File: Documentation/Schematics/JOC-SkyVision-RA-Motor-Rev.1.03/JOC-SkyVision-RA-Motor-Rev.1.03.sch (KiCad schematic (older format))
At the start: 18 parts, among them CON1 Conn_01x02_Male, CON2 Conn_01x02_Male, J1 RJ45, J2 RJ45, J3 RJ12 (ST-04 Guiding Port), Q1 4947A Dual P-Channel Mosfet, Q2 4936A Dual N-Channel Mosfet, U1 PIC16F690-ISO, U2_LED Motor Encoder LED, U2_PD Motor Encoder Photodiodes, U3 AZ1117-5.0 (GH15E), U4 TC4426A, X1 20 MHz Crystal

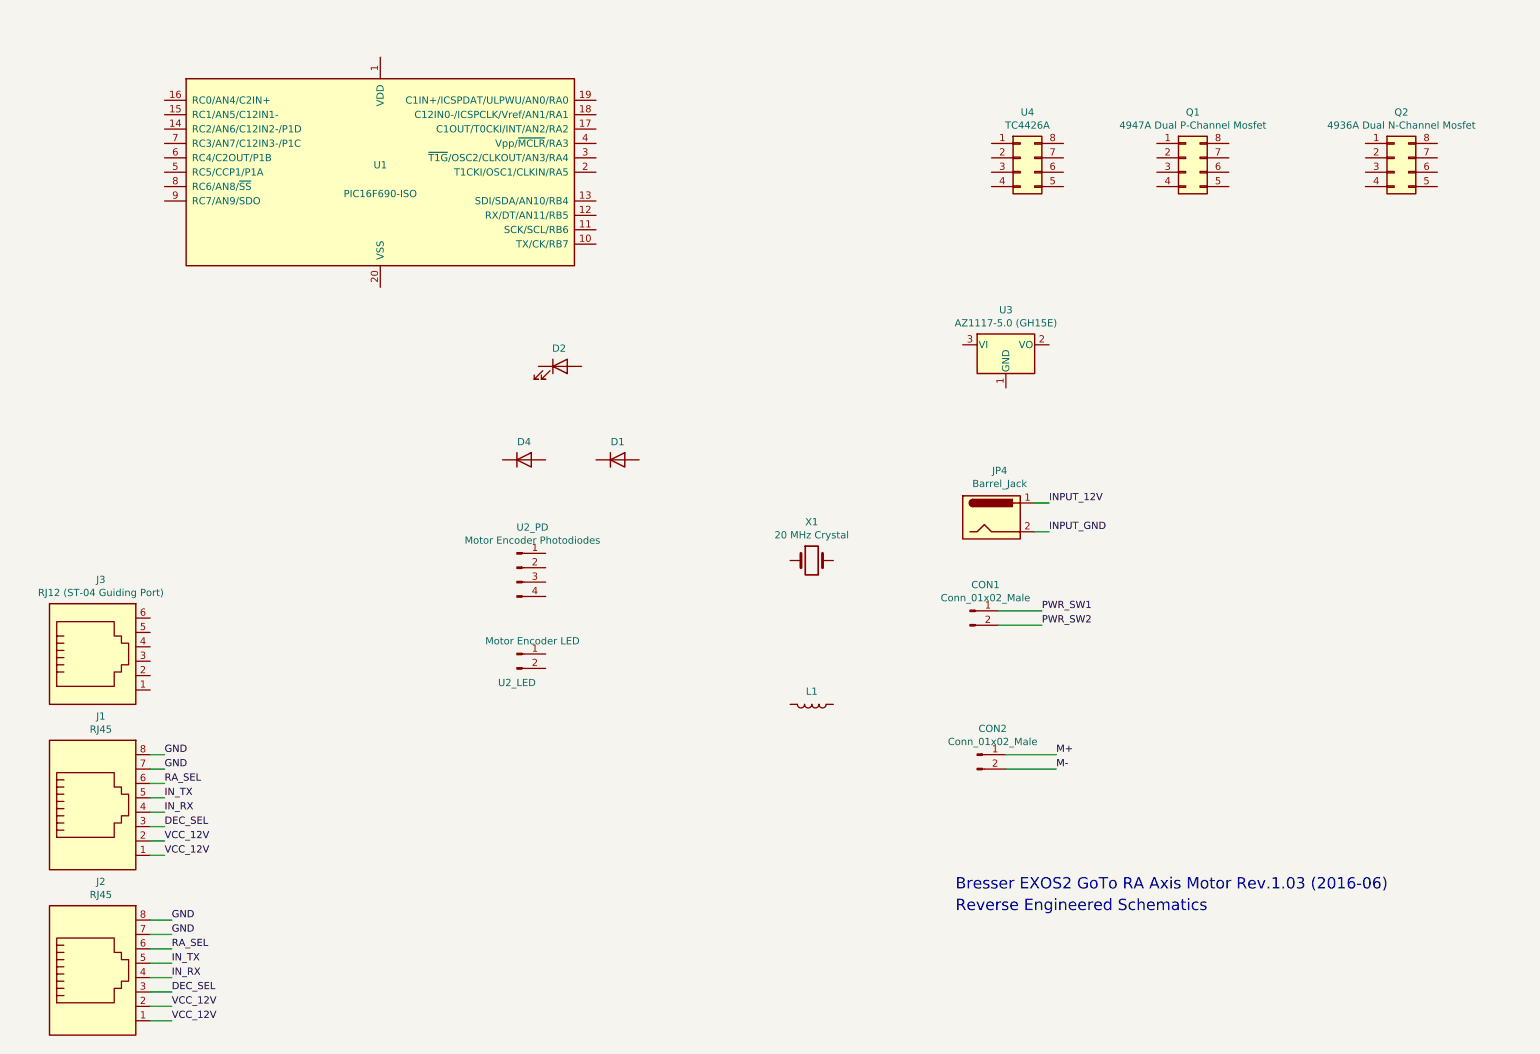
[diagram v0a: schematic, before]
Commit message: Added RA Motor data sheets
updated DEC motor wrong polarity on mosfets :o
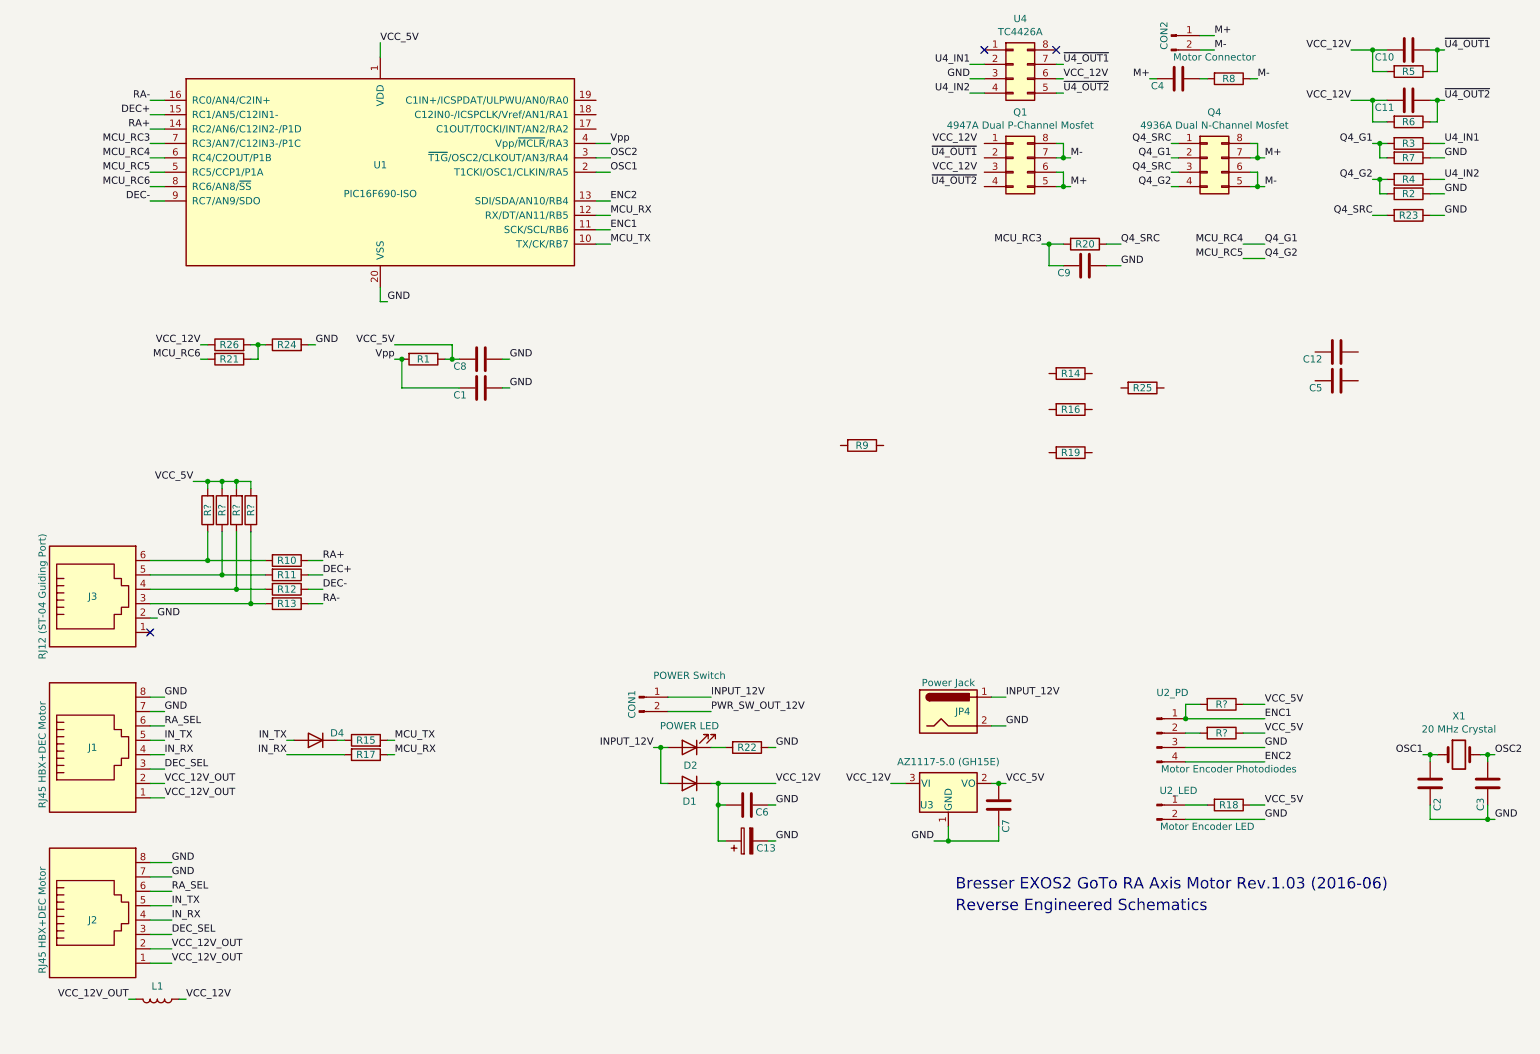
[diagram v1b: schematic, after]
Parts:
- added C1, C10, C11, C12, C2, C3, C4, C5, C6, C7, C8, C9: C, symbol Device:C
- added C13: C, symbol Device:CP
- added R1, R10, R11, R12, R13, R14, R15, R16, R17, R18, R19, R2, R20, R21, R22, R23, R24, R25, R26, R3, R4, R5, R6, R7, R8, R9, R? (x6): R, symbol Device:R
- CON1: value Conn_01x02_Male -> POWER Switch
- CON2: value Conn_01x02_Male -> Motor Connector
- D2: value LED -> POWER LED
- J1, J2: value RJ45 -> RJ45 HBX+DEC Motor
- JP4: value Barrel_Jack -> Power Jack
- renumbered Q2 to Q4
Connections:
- net INPUT_GND is gone; now on net GND: JP4.2
- net PWR_SW1 is gone; now on net INPUT_12V: CON1.1 (Pin_1)
- net GND: now also J3.2, U1.20 (VSS), U2_LED.2 (Pin_2), U2_PD.3 (Pin_3), U3.1 (GND), U4.3 (Pin_3), C1.2, C13.2, C2.1, C3.1, C6.2, C7.1, C8.2, C9.2, R2.1, R22.1, R23.1, R24.2, R7.1
- net INPUT_12V: now also D1.2 (A), D2.2 (A)
- net IN_RX: now also R17.2
- net IN_TX: now also D4.2 (A)
- net M+: now also Q1.5 (Pin_5), Q1.6 (Pin_6), Q4.7 (Pin_7), Q4.8 (Pin_8), C4.1
- net M-: now also Q1.7 (Pin_7), Q1.8 (Pin_8), Q4.5 (Pin_5), Q4.6 (Pin_6), R8.1
- net VCC_12V: now also D1.1 (K), L1.1, U3.3 (VI), U4.6 (Pin_6), C10.1, C11.1, C13.1, C6.1, R26.1, R5.2, R6.2; no longer J1.1, J1.2, J2.1, J2.2
- net VCC_5V: now reaches U1.1 (VDD)
- net VCC_5V: now also U3.2 (VO), C7.2, C8.1, R1.1, R18.1, R?.1, R?.1, R?.2, R?.2, R?.2, R?.2
- net MCU_TX: now reaches U1.10 (TX/CK/RB7)
- net MCU_TX: now also R15.2
- net ENC1: now reaches U1.11 (SCK/SCL/RB6)
- net ENC1: now also U2_PD.1 (Pin_1), R?.2
- net MCU_RX: now reaches U1.12 (RX/DT/AN11/RB5)
- net MCU_RX: now also R17.1
- net ENC2: now reaches U1.13 (SDI/SDA/AN10/RB4)
- net ENC2: now also U2_PD.4 (Pin_4)
- net RA+: now reaches U1.14 (RC2/AN6/C12IN2-/P1D)
- net RA+: now also R10.1
- net DEC+: now reaches U1.15 (RC1/AN5/C12IN1-)
- net DEC+: now also R11.1
- net RA-: now reaches U1.16 (RC0/AN4/C2IN+)
- net RA-: now also R13.1
- net OSC1: now reaches U1.2 (T1CKI/OSC1/CLKIN/RA5)
- net OSC1: now also X1.1, C2.2
- net OSC2: now reaches U1.3 (~T1G~/OSC2/CLKOUT/AN3/RA4)
- net OSC2: now also X1.2, C3.2
- net Vpp: now reaches U1.4 (Vpp/~MCLR~/RA3)
- net Vpp: now also C1.1, R1.2
- net MCU_RC5: now reaches U1.5 (RC5/CCP1/P1A)
- net MCU_RC5: now also Q4.4 (Pin_4), R2.2, R4.2
- net MCU_RC4: now reaches U1.6 (RC4/C2OUT/P1B)
- net MCU_RC4: now also Q4.2 (Pin_2), R3.2, R7.2
- net MCU_RC3: now reaches U1.7 (RC3/AN7/C12IN3-/P1C)
- net MCU_RC3: now also C9.1, R20.2
- net MCU_RC6: now reaches U1.8 (RC6/AN8/~SS~)
- net MCU_RC6: now also R21.2
- net DEC-: now reaches U1.9 (RC7/AN9/SDO)
- net DEC-: now also R12.1
- net U4_IN1: now reaches U4.2 (Pin_2)
- net U4_IN1: now also R3.1
- net U4_IN2: now reaches U4.4 (Pin_4)
- net U4_IN2: now also R4.1
- net ~U4_OUT2: now reaches U4.5 (Pin_5)
- net ~U4_OUT2: now also C11.2, R6.1
- net ~U4_OUT1: now reaches U4.7 (Pin_7)
- net ~U4_OUT1: now also C10.2, R5.1
- net Q4_SRC: now reaches Q4.1 (Pin_1)
- net Q4_SRC: now also Q4.3 (Pin_3), R20.1, R23.2
- net at U2_PD.2 (Pin_2): now also R?.2
- net at U2_LED.1 (Pin_1): now also R18.2
- net VCC_12V_OUT: now reaches L1.2
- net VCC_12V_OUT: now also J1.1, J1.2, J2.1, J2.2
- net at D4.1 (K): now also R15.1
- net at D2.1 (K): now also R22.2
- net at J3.3: now also R13.2, R?.1
- net at J3.4: now also R12.2, R?.1
- net at J3.5: now also R11.2, R?.1
- net at J3.6: now also R10.2, R?.1
- net PWR_SW2 renamed PWR_SW_OUT_12V
- new net: C4.2, R8.2
- new net: R21.1, R24.1, R26.2
- no-connect marks 0 -> 3
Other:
- moved on the sheet: CON1, CON2, D1, D2, D4, J1, J2, J3, JP4, L1, Q1, Q4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

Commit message: updated schematics
added introduction text for schematics
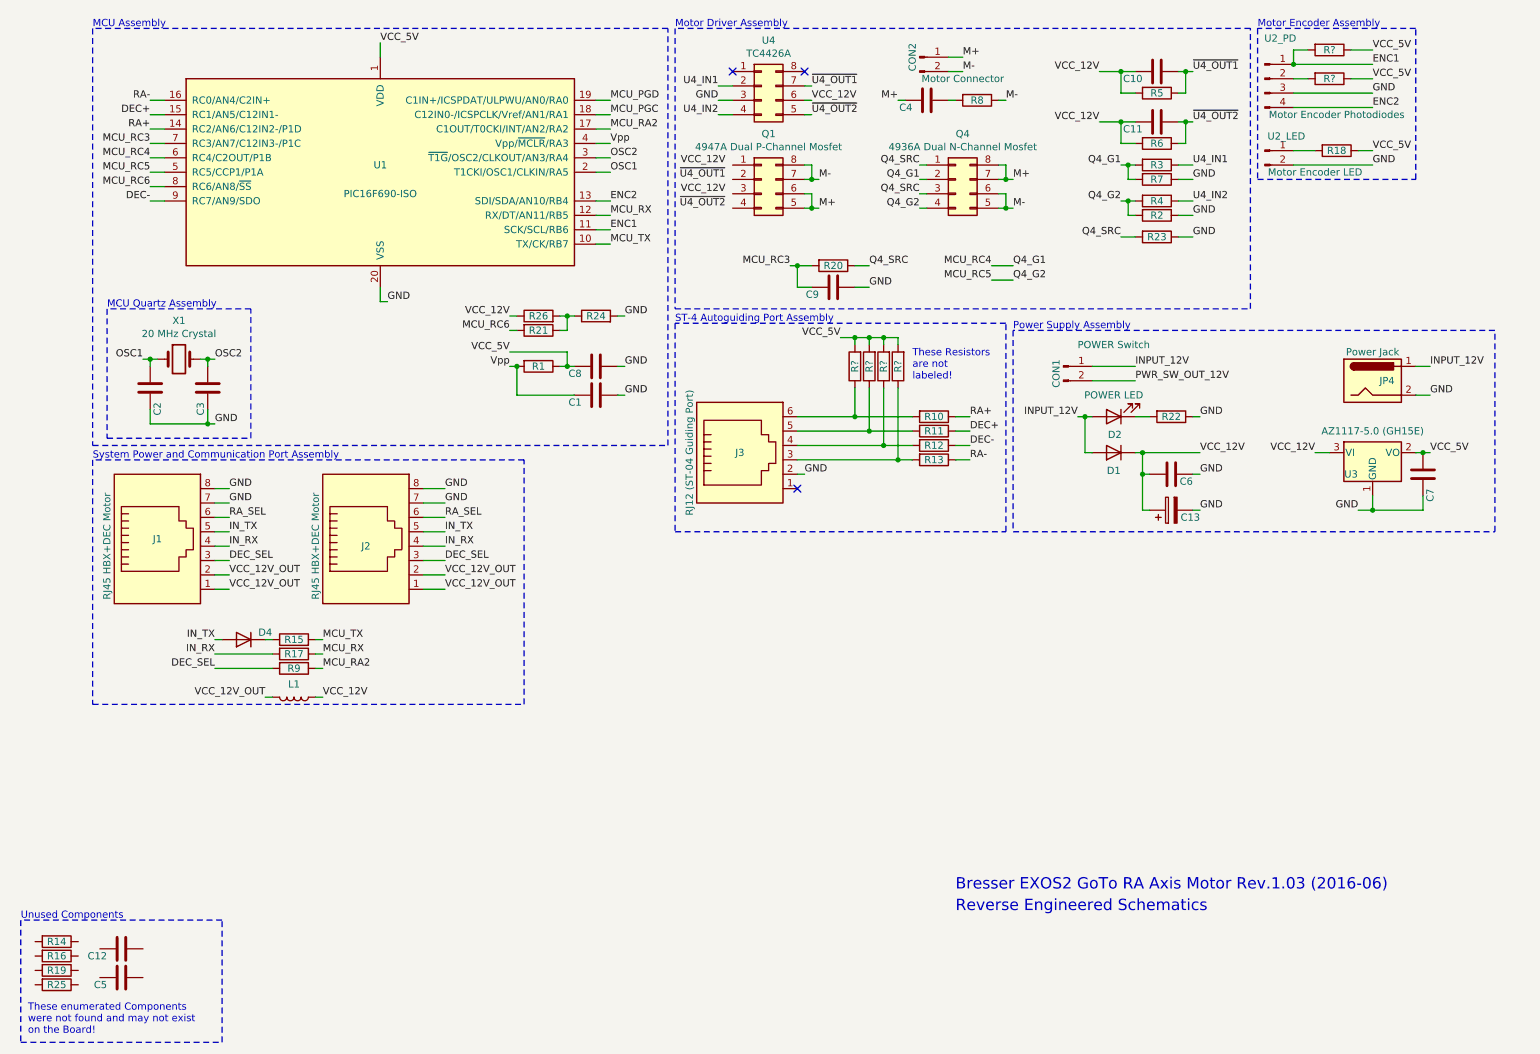
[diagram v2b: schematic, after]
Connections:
- net DEC_SEL: now also R9.2
- net MCU_RA2: now reaches U1.17 (C1OUT/T0CKI/INT/AN2/RA2)
- net MCU_RA2: now also R9.1
- net MCU_PGC: now reaches U1.18 (C12IN0-/ICSPCLK/Vref/AN1/RA1)
- net MCU_PGD: now reaches U1.19 (C1IN+/ICSPDAT/ULPWU/AN0/RA0)
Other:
- note added: "MCU Assembly"
- note added: "MCU Quartz Assembly"
- note added: "Motor Driver Assembly"
- note added: "Motor Encoder Assembly"
- note added: "Power Supply Assembly"
- note added: "ST-4 Autoguiding Port Assembly"
- note added: "System Power and Communication Port Assembly"
- note added: "These Resistors\nare not\nlabeled!"
- note added: "These enumerated Components\nwere not found and may not exist\non the Board!"
- note added: "Unused Components"
- moved on the sheet: C1, C10, C11, C12, C13, C2, C3, C4, C5, C6, C7, C8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
